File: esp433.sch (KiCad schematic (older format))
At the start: 52 parts, among them J1 USB_OTG, J2 CONN_01X03, Q1 MBT2222ADW1T1, SW1 SW_Push, U1 IRM-02-5, U2 AP2127K-3.3, U3 MAX7044, U4 ESP-12E, U5 FT231XS, Y1 Crystal

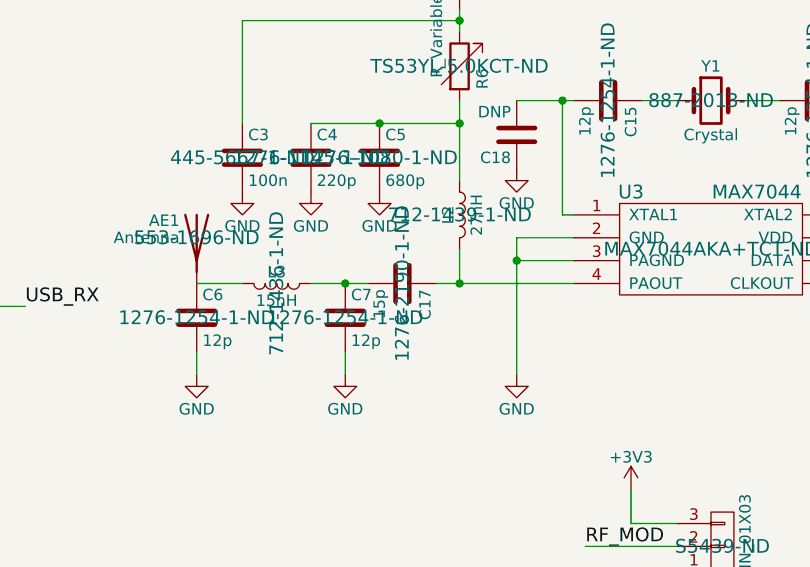
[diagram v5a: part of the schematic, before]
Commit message: Pick inductors specified by MAX7044 reference design
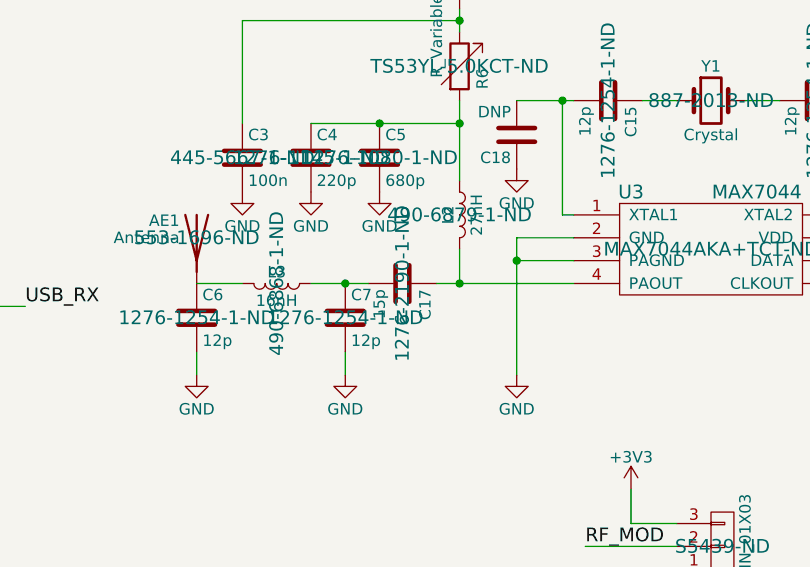
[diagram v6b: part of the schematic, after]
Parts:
- L2: Vendorpart 712-1439-1-ND -> 490-6879-1-ND
- L3: value 15nH -> 16nH; Vendorpart 712-1436-1-ND -> 490-6868-1-ND
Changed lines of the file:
@@
 $EndComp
 $Comp
-L GND #PWR9
+L GND #PWR01
 U 1 1 5A6C1DE7
 P 4850 2650
-F 0 "#PWR9" H 4850 2400 50  0001 C CNN
+F 0 "#PWR01" H 4850 2400 50  0001 C CNN
 F 1 "GND" H 4850 2500 50  0000 C CNN
 F 2 "" H 4850 2650 50  0001 C CNN
@@
 $EndComp
 $Comp
-L +3V3 #PWR5
+L +3V3 #PWR02
 U 1 1 5A6C1E2B
 P 5500 1650
-F 0 "#PWR5" H 5500 1500 50  0001 C CNN
+F 0 "#PWR02" H 5500 1500 50  0001 C CNN
 F 1 "+3V3" H 5500 1790 50  0000 C CNN
 F 2 "" H 5500 1650 50  0001 C CNN
@@
 $EndComp
 $Comp
-L +5V #PWR4
+L +5V #PWR03
 U 1 1 5A6C1E6F
 P 4350 1650
-F 0 "#PWR4" H 4350 1500 50  0001 C CNN
+F 0 "#PWR03" H 4350 1500 50  0001 C CNN
 F 1 "+5V" H 4350 1790 50  0000 C CNN
 F 2 "" H 4350 1650 50  0001 C CNN
@@
 $EndComp
 $Comp
-L +3V3 #PWR1
+L +3V3 #PWR04
 U 1 1 5A6C1EEB
 P 9550 1350
-F 0 "#PWR1" H 9550 1200 50  0001 C CNN
+F 0 "#PWR04" H 9550 1200 50  0001 C CNN
 F 1 "+3V3" H 9550 1490 50  0000 C CNN
 F 2 "" H 9550 1350 50  0001 C CNN
@@
 $EndComp
 $Comp
-L +3V3 #PWR2
+L +3V3 #PWR05
 U 1 1 5A6C1F26
 P 10000 1350
-F 0 "#PWR2" H 10000 1200 50  0001 C CNN
+F 0 "#PWR05" H 10000 1200 50  0001 C CNN
 F 1 "+3V3" H 10000 1490 50  0000 C CNN
 F 2 "" H 10000 1350 50  0001 C CNN
@@
 GPIO0
 $Comp
-L GND #PWR31
+L GND #PWR06
 U 1 1 5A6D5837
 P 9150 5550
-F 0 "#PWR31" H 9150 5300 50  0001 C CNN
+F 0 "#PWR06" H 9150 5300 50  0001 C CNN
 F 1 "GND" H 9150 5400 50  0000 C CNN
 F 2 "" H 9150 5550 50  0001 C CNN
@@
 $EndComp
 $Comp
-L +3V3 #PWR30
+L +3V3 #PWR07
 U 1 1 5A6D58FF
 P 7600 5400
-F 0 "#PWR30" H 7600 5250 50  0001 C CNN
+F 0 "#PWR07" H 7600 5250 50  0001 C CNN
 F 1 "+3V3" H 7600 5540 50  0000 C CNN
 F 2 "" H 7600 5400 50  0001 C CNN
@@
 GPIO15
 $Comp
-L GND #PWR7
+L GND #PWR08
 U 1 1 5A6D5ED0
 P 10400 2050
-F 0 "#PWR7" H 10400 1800 50  0001 C CNN
+F 0 "#PWR08" H 10400 1800 50  0001 C CNN
 F 1 "GND" H 10400 1900 50  0000 C CNN
 F 2 "" H 10400 2050 50  0001 C CNN
@@
 $EndComp
 $Comp
-L +3V3 #PWR17
+L +3V3 #PWR09
 U 1 1 5A6D623C
 P 3850 3450
-F 0 "#PWR17" H 3850 3300 50  0001 C CNN
+F 0 "#PWR09" H 3850 3300 50  0001 C CNN
 F 1 "+3V3" H 3850 3590 50  0000 C CNN
 F 2 "" H 3850 3450 50  0001 C CNN
@@
 $EndComp
 $Comp
-L GND #PWR26
+L GND #PWR010
 U 1 1 5A6D62B4
 P 6050 4700
-F 0 "#PWR26" H 6050 4450 50  0001 C CNN
+F 0 "#PWR010" H 6050 4450 50  0001 C CNN
 F 1 "GND" H 6050 4550 50  0000 C CNN
 F 2 "" H 6050 4700 50  0001 C CNN
@@
 $EndComp
 $Comp
-L +5V #PWR27
+L +5V #PWR011
 U 1 1 5A6D6578
 P 3000 5050
-F 0 "#PWR27" H 3000 4900 50  0001 C CNN
+F 0 "#PWR011" H 3000 4900 50  0001 C CNN
 F 1 "+5V" H 3000 5190 50  0000 C CNN
 F 2 "" H 3000 5050 50  0001 C CNN
@@
 $EndComp
 $Comp
-L GND #PWR35
+L GND #PWR012
 U 1 1 5A6D65B9
 P 3000 7200
-F 0 "#PWR35" H 3000 6950 50  0001 C CNN
+F 0 "#PWR012" H 3000 6950 50  0001 C CNN
 F 1 "GND" H 3000 7050 50  0000 C CNN
 F 2 "" H 3000 7200 50  0001 C CNN
@@
 $EndComp
 $Comp
-L GND #PWR36
+L GND #PWR013
 U 1 1 5A6D65FA
 P 3200 7200
-F 0 "#PWR36" H 3200 6950 50  0001 C CNN
+F 0 "#PWR013" H 3200 6950 50  0001 C CNN
 F 1 "GND" H 3200 7050 50  0000 C CNN
 F 2 "" H 3200 7200 50  0001 C CNN
@@
 $EndComp
 $Comp
-L +5V #PWR11
+L +5V #PWR014
 U 1 1 5A6D6D35
 P 2650 3100
-F 0 "#PWR11" H 2650 2950 50  0001 C CNN
+F 0 "#PWR014" H 2650 2950 50  0001 C CNN
 F 1 "+5V" H 2650 3240 50  0000 C CNN
 F 2 "" H 2650 3100 50  0001 C CNN
@@
 $EndComp
 $Comp
-L GND #PWR18
+L GND #PWR015
 U 1 1 5A6D6EA9
 P 1550 4050
-F 0 "#PWR18" H 1550 3800 50  0001 C CNN
+F 0 "#PWR015" H 1550 3800 50  0001 C CNN
 F 1 "GND" H 1550 3900 50  0000 C CNN
 F 2 "" H 1550 4050 50  0001 C CNN
@@
 $EndComp
 $Comp
-L GND #PWR6
+L GND #PWR016
 U 1 1 5A6D85B9
 P 2650 1850
-F 0 "#PWR6" H 2650 1600 50  0001 C CNN
+F 0 "#PWR016" H 2650 1600 50  0001 C CNN
 F 1 "GND" H 2650 1700 50  0000 C CNN
 F 2 "" H 2650 1850 50  0001 C CNN
@@
 $EndComp
 $Comp
-L +5V #PWR3
+L +5V #PWR017
 U 1 1 5A6D867B
 P 3200 1500
-F 0 "#PWR3" H 3200 1350 50  0001 C CNN
+F 0 "#PWR017" H 3200 1350 50  0001 C CNN
 F 1 "+5V" H 3200 1640 50  0000 C CNN
 F 2 "" H 3200 1500 50  0001 C CNN
@@
 $EndComp
 $Comp
-L +3V3 #PWR32
+L +3V3 #PWR018
 U 1 1 5A6D9A1C
 P 5900 5700
-F 0 "#PWR32" H 5900 5550 50  0001 C CNN
+F 0 "#PWR018" H 5900 5550 50  0001 C CNN
 F 1 "+3V3" H 5900 5840 50  0000 C CNN
 F 2 "" H 5900 5700 50  0001 C CNN
@@
 $EndComp
 $Comp
-L +3V3 #PWR25
+L +3V3 #PWR019
 U 1 1 5A6DA721
 P 9250 4600
-F 0 "#PWR25" H 9250 4450 50  0001 C CNN
+F 0 "#PWR019" H 9250 4450 50  0001 C CNN
 F 1 "+3V3" H 9250 4740 50  0000 C CNN
 F 2 "" H 9250 4600 50  0001 C CNN
@@
 $EndComp
 $Comp
-L GND #PWR29
+L GND #PWR020
 U 1 1 5A6DA77A
 P 9250 5100
-F 0 "#PWR29" H 9250 4850 50  0001 C CNN
+F 0 "#PWR020" H 9250 4850 50  0001 C CNN
 F 1 "GND" H 9250 4950 50  0000 C CNN
 F 2 "" H 9250 5100 50  0001 C CNN
@@
 $EndComp
 $Comp
-L GND #PWR24
+L GND #PWR021
 U 1 1 5A6DD0A2
 P 2650 4400
-F 0 "#PWR24" H 2650 4150 50  0001 C CNN
+F 0 "#PWR021" H 2650 4150 50  0001 C CNN
 F 1 "GND" H 2650 4250 50  0000 C CNN
 F 2 "" H 2650 4400 50  0001 C CNN
@@
 $EndComp
 $Comp
-L GND #PWR23
+L GND #PWR022
 U 1 1 5A6DD462
 P 2000 4400
-F 0 "#PWR23" H 2000 4150 50  0001 C CNN
+F 0 "#PWR022" H 2000 4150 50  0001 C CNN
 F 1 "GND" H 2000 4250 50  0000 C CNN
 F 2 "" H 2000 4400 50  0001 C CNN
@@
 $EndComp
 $Comp
-L +5V #PWR33
+L +5V #PWR023
 U 1 1 5A6DE01F
 P 1650 6550
-F 0 "#PWR33" H 1650 6400 50  0001 C CNN
+F 0 "#PWR023" H 1650 6400 50  0001 C CNN
 F 1 "+5V" H 1650 6690 50  0000 C CNN
 F 2 "" H 1650 6550 50  0001 C CNN
@@
 $EndComp
 $Comp
-L GND #PWR34
+L GND #PWR024
 U 1 1 5A6DE1A7
 P 1650 7150
-F 0 "#PWR34" H 1650 6900 50  0001 C CNN
+F 0 "#PWR024" H 1650 6900 50  0001 C CNN
 F 1 "GND" H 1650 7000 50  0000 C CNN
 F 2 "" H 1650 7150 50  0001 C CNN
@@
 AC-N
 $Comp
-L +3V3 #PWR28
+L +3V3 #PWR025
 U 1 1 5A6D6537
 P 3200 5050
-F 0 "#PWR28" H 3200 4900 50  0001 C CNN
+F 0 "#PWR025" H 3200 4900 50  0001 C CNN
 F 1 "+3V3" H 3200 5190 50  0000 C CNN
 F 2 "" H 3200 5050 50  0001 C CNN
@@
 $EndComp
 $Comp
-L GND #PWR22
+L GND #PWR026
 U 1 1 5A766445
 P 10350 4150
-F 0 "#PWR22" H 10350 3900 50  0001 C CNN
+F 0 "#PWR026" H 10350 3900 50  0001 C CNN
 F 1 "GND" H 10350 4000 50  0000 C CNN
 F 2 "" H 10350 4150 50  0001 C CNN
@@
 $EndComp
 $Comp
-L +3V3 #PWR10
+L +3V3 #PWR027
 U 1 1 5A7665C1
 P 10350 2800
-F 0 "#PWR10" H 10350 2650 50  0001 C CNN
+F 0 "#PWR027" H 10350 2650 50  0001 C CNN
 F 1 "+3V3" H 10350 2940 50  0000 C CNN
 F 2 "" H 10350 2800 50  0001 C CNN
@@
 $EndComp
 $Comp
-L GND #PWR21
+L GND #PWR028
 U 1 1 5A7669B1
 P 8750 4100
-F 0 "#PWR21" H 8750 3850 50  0001 C CNN
+F 0 "#PWR028" H 8750 3850 50  0001 C CNN
 F 1 "GND" H 8750 3950 50  0000 C CNN
 F 2 "" H 8750 4100 50  0001 C CNN
@@
 $EndComp
 $Comp
-L +3V3 #PWR8
+L +3V3 #PWR029
 U 1 1 5A767193
 P 8500 2500
-F 0 "#PWR8" H 8500 2350 50  0001 C CNN
+F 0 "#PWR029" H 8500 2350 50  0001 C CNN
 F 1 "+3V3" H 8500 2640 50  0000 C CNN
 F 2 "" H 8500 2500 50  0001 C CNN
@@
 F 2 "Inductors_SMD:L_0603" H 8500 3400 50  0001 C CNN
 F 3 "" H 8500 3400 50  0001 C CNN
-F 4 "712-1439-1-ND" H 8500 3400 60  0000 C CNN "Vendorpart"
+F 4 "490-6879-1-ND" H 8500 3400 60  0000 C CNN "Vendorpart"
 	1    8500 3400
 	1    0    0    -1
@@
 P 7700 3700
 F 0 "L3" V 7650 3700 50  0000 C CNN
-F 1 "15nH" V 7775 3700 50  0000 C CNN
+F 1 "16nH" V 7775 3700 50  0000 C CNN
 F 2 "Inductors_SMD:L_0603" H 7700 3700 50  0001 C CNN
 F 3 "" H 7700 3700 50  0001 C CNN
-F 4 "712-1436-1-ND" H 7700 3700 60  0000 C CNN "Vendorpart"
+F 4 "490-6868-1-ND" H 7700 3700 60  0000 C CNN "Vendorpart"
 	1    7700 3700
 	0    1    1    0
@@
 $EndComp
 $Comp
-L GND #PWR20
+L GND #PWR030
 U 1 1 5A767EA9
 P 8000 4100
-F 0 "#PWR20" H 8000 3850 50  0001 C CNN
+F 0 "#PWR030" H 8000 3850 50  0001 C CNN
 F 1 "GND" H 8000 3950 50  0000 C CNN
 F 2 "" H 8000 4100 50  0001 C CNN
@@
 $EndComp
 $Comp
-L GND #PWR19
+L GND #PWR031
 U 1 1 5A767F41
 P 7350 4100
-F 0 "#PWR19" H 7350 3850 50  0001 C CNN
+F 0 "#PWR031" H 7350 3850 50  0001 C CNN
 F 1 "GND" H 7350 3950 50  0000 C CNN
 F 2 "" H 7350 4100 50  0001 C CNN
@@
 RF_CLK
 $Comp
-L GND #PWR16
+L GND #PWR032
 U 1 1 5A769625
 P 8150 3300
-F 0 "#PWR16" H 8150 3050 50  0001 C CNN
+F 0 "#PWR032" H 8150 3050 50  0001 C CNN
 F 1 "GND" H 8150 3150 50  0000 C CNN
 F 2 "" H 8150 3300 50  0001 C CNN
@@
 $EndComp
 $Comp
-L GND #PWR15
+L GND #PWR033
 U 1 1 5A7696BD
 P 7850 3300
-F 0 "#PWR15" H 7850 3050 50  0001 C CNN
+F 0 "#PWR033" H 7850 3050 50  0001 C CNN
 F 1 "GND" H 7850 3150 50  0000 C CNN
 F 2 "" H 7850 3300 50  0001 C CNN
@@
 $EndComp
 $Comp
-L GND #PWR14
+L GND #PWR034
 U 1 1 5A769755
 P 7550 3300
-F 0 "#PWR14" H 7550 3050 50  0001 C CNN
+F 0 "#PWR034" H 7550 3050 50  0001 C CNN
 F 1 "GND" H 7550 3150 50  0000 C CNN
 F 2 "" H 7550 3300 50  0001 C CNN
@@
 Connection ~ 10250 2900
 $Comp
-L GND #PWR12
+L GND #PWR035
 U 1 1 5A91ADD1
 P 8750 3200
-F 0 "#PWR12" H 8750 2950 50  0001 C CNN
+F 0 "#PWR035" H 8750 2950 50  0001 C CNN
 F 1 "GND" H 8750 3050 50  0000 C CNN
 F 2 "" H 8750 3200 50  0001 C CNN
@@
 $EndComp
 $Comp
-L GND #PWR13
+L GND #PWR036
 U 1 1 5A91AE7B
 P 10600 3200
-F 0 "#PWR13" H 10600 2950 50  0001 C CNN
+F 0 "#PWR036" H 10600 2950 50  0001 C CNN
 F 1 "GND" H 10600 3050 50  0000 C CNN
 F 2 "" H 10600 3200 50  0001 C CNN

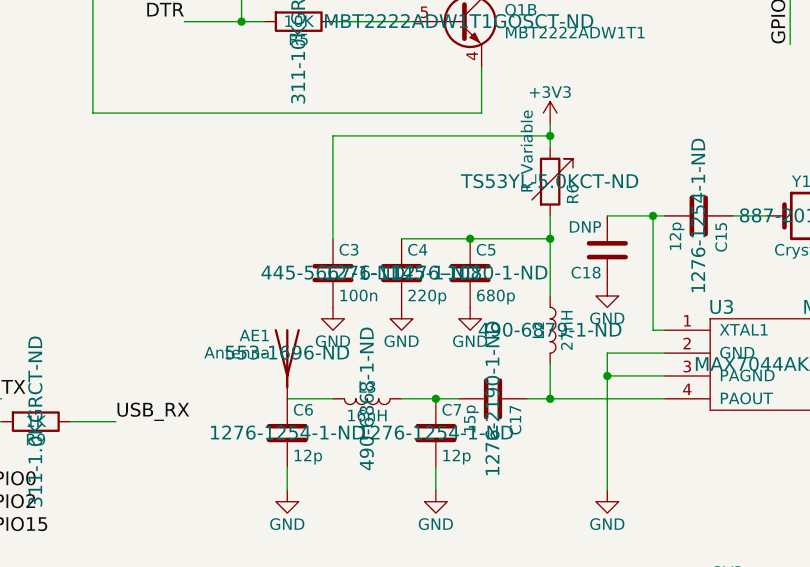
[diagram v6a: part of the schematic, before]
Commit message: More parts to match reference design
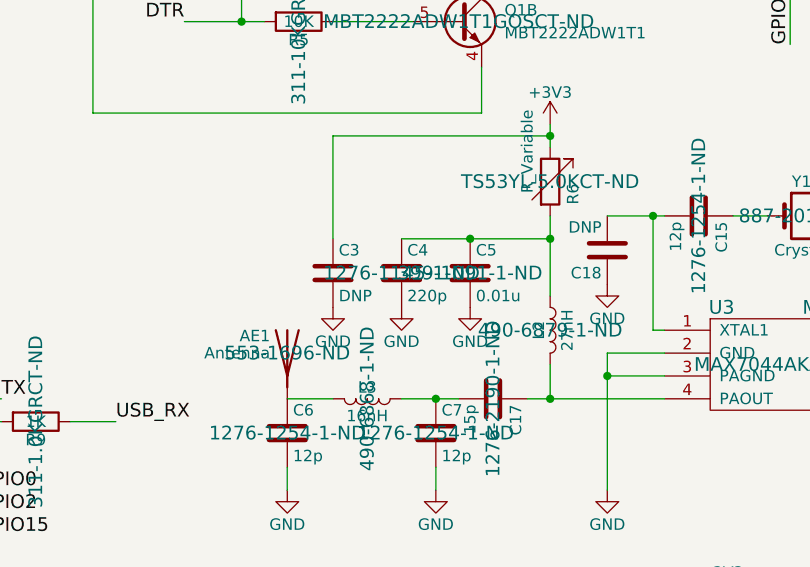
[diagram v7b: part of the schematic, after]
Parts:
- C3: value 100n -> DNP; Vendorpart 445-5667-1-ND -> (none)
- C5: value 680p -> 0.01u; Vendorpart 1276-1080-1-ND -> 399-1091-1-ND
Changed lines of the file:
@@
 P 7550 3150
 F 0 "C3" H 7575 3250 50  0000 L CNN
-F 1 "100n" H 7575 3050 50  0000 L CNN
+F 1 "DNP" H 7575 3050 50  0000 L CNN
 F 2 "Capacitors_SMD:C_0603" H 7588 3000 50  0001 C CNN
 F 3 "" H 7550 3150 50  0001 C CNN
-F 4 "445-5667-1-ND" H 7550 3150 60  0000 C CNN "Vendorpart"
 	1    7550 3150
 	1    0    0    -1
@@
 P 8150 3150
 F 0 "C5" H 8175 3250 50  0000 L CNN
-F 1 "680p" H 8175 3050 50  0000 L CNN
+F 1 "0.01u" H 8175 3050 50  0000 L CNN
 F 2 "Capacitors_SMD:C_0603" H 8188 3000 50  0001 C CNN
 F 3 "" H 8150 3150 50  0001 C CNN
-F 4 "1276-1080-1-ND" H 8150 3150 60  0000 C CNN "Vendorpart"
+F 4 "399-1091-1-ND" H 8150 3150 60  0000 C CNN "Vendorpart"
 	1    8150 3150
 	1    0    0    -1
